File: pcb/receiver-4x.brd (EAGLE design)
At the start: 76.2 x 50.8 mm, 26 parts, among them IC1 MAX3095CEE

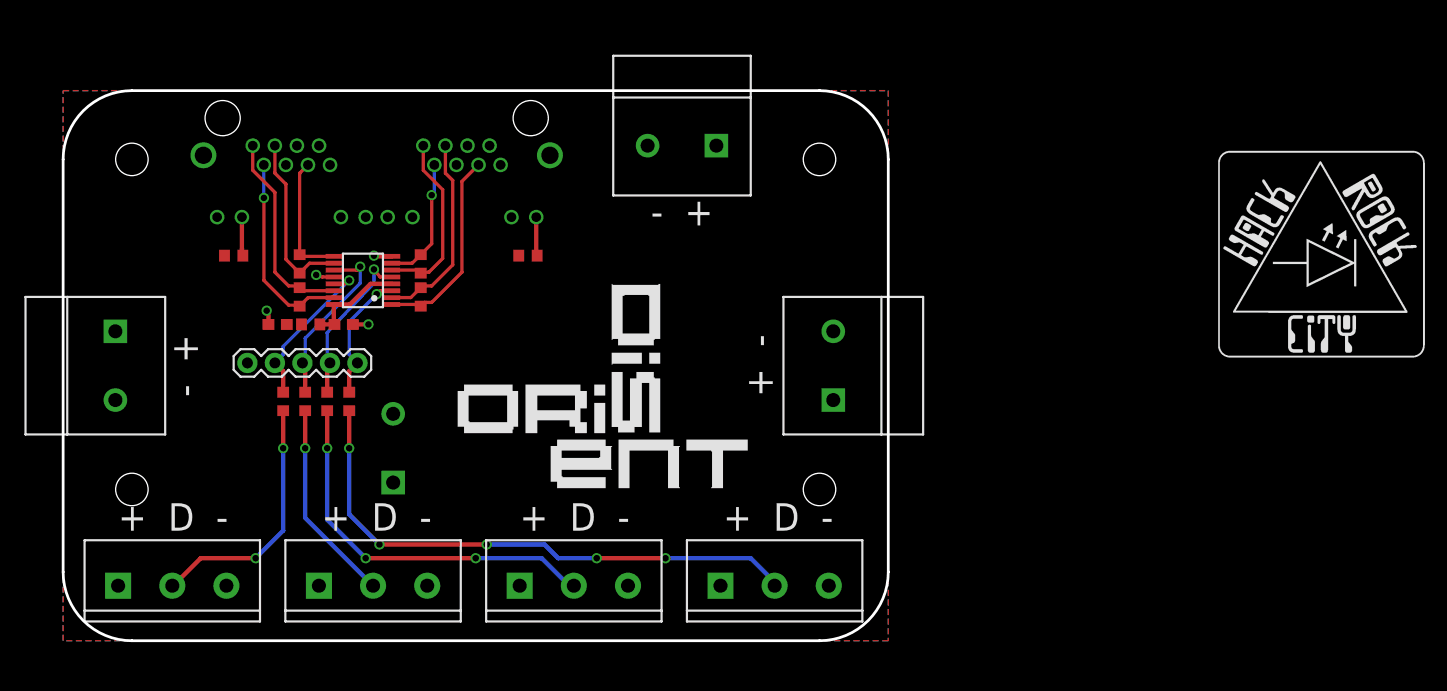
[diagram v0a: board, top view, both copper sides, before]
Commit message: Receiver 4x: Rev B design
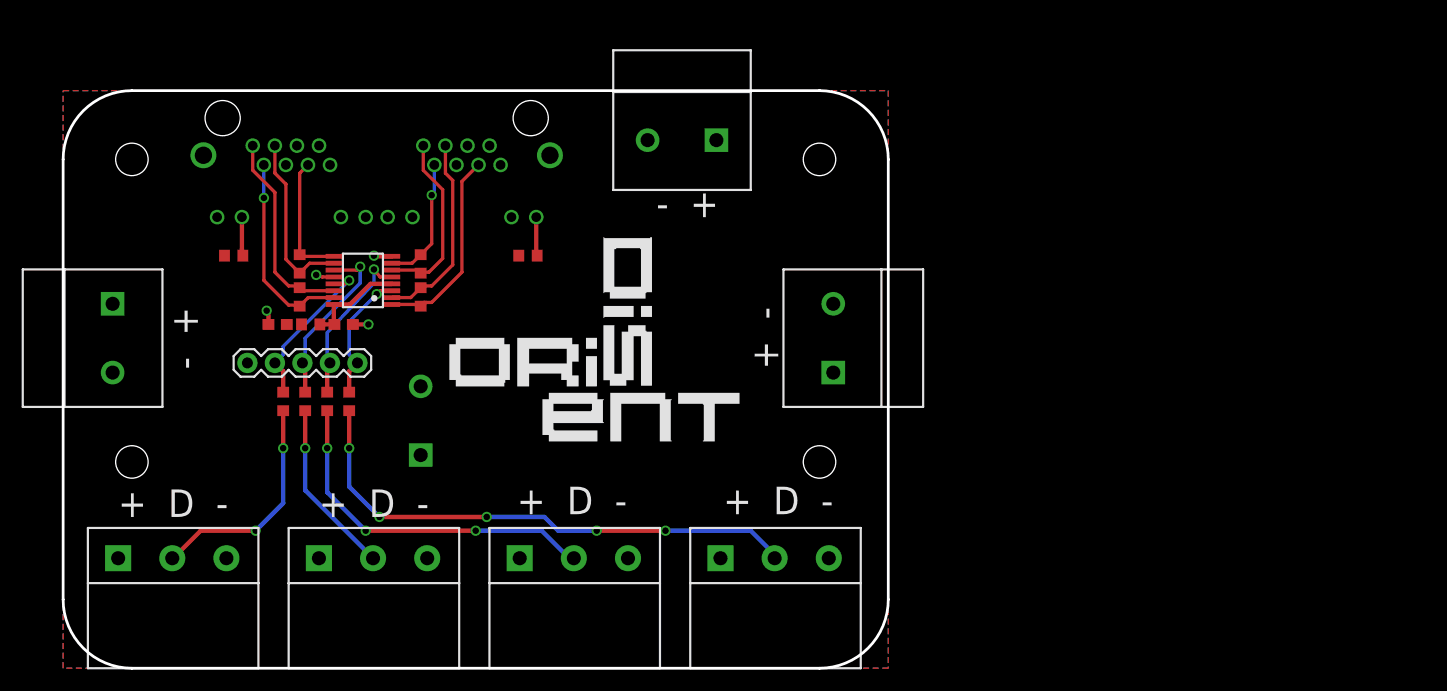
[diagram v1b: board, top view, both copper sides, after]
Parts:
- removed U$4: (no value), naim_misc:HRC_LOGO_0.75IN
- JP1, JP2, JP3, JP4: device SparkFun-Connectors:SCREWTERMINAL-5MM-3 -> LEDscape:SCREWTERMINAL-5MM-3-DETACHABLE
- moved U$3 4.38 mm to (49.5, 25.9)
- moved JP12 3.59 mm to (33.0, 20.3)
- moved JP5 2.55 mm to (4.57, 27.9)
- moved JP9 2.54 mm to (71.1, 27.9)
- moved JP1 2.54 mm to (60.7, 7.62)
- moved JP2 2.54 mm to (42.2, 7.62)
- moved JP3 2.54 mm to (23.6, 7.62)
- moved JP4 2.54 mm to (5.08, 7.62)
- moved JP10 0.51 mm to (57.1, 46.2)
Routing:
- net N$6: track 23.4 -> 20.9 mm
- net N$5: track 18.8 -> 16.2 mm
- net N$4: track 35.4 -> 32.8 mm
- net N$1: track 51.8 -> 49.2 mm
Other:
- board size 76.2 x 50.8 mm -> 76.2 x 53.3 mm
- board text added: "LEDscape receiver Rev B 2014-09-2 By Matt Mets"
- board text removed: "RS485 receiver Rev B 2014-09-1 @cibomahto"

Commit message: Updated BBB footprint, mounting holes in LEDscape baord, small cleanups
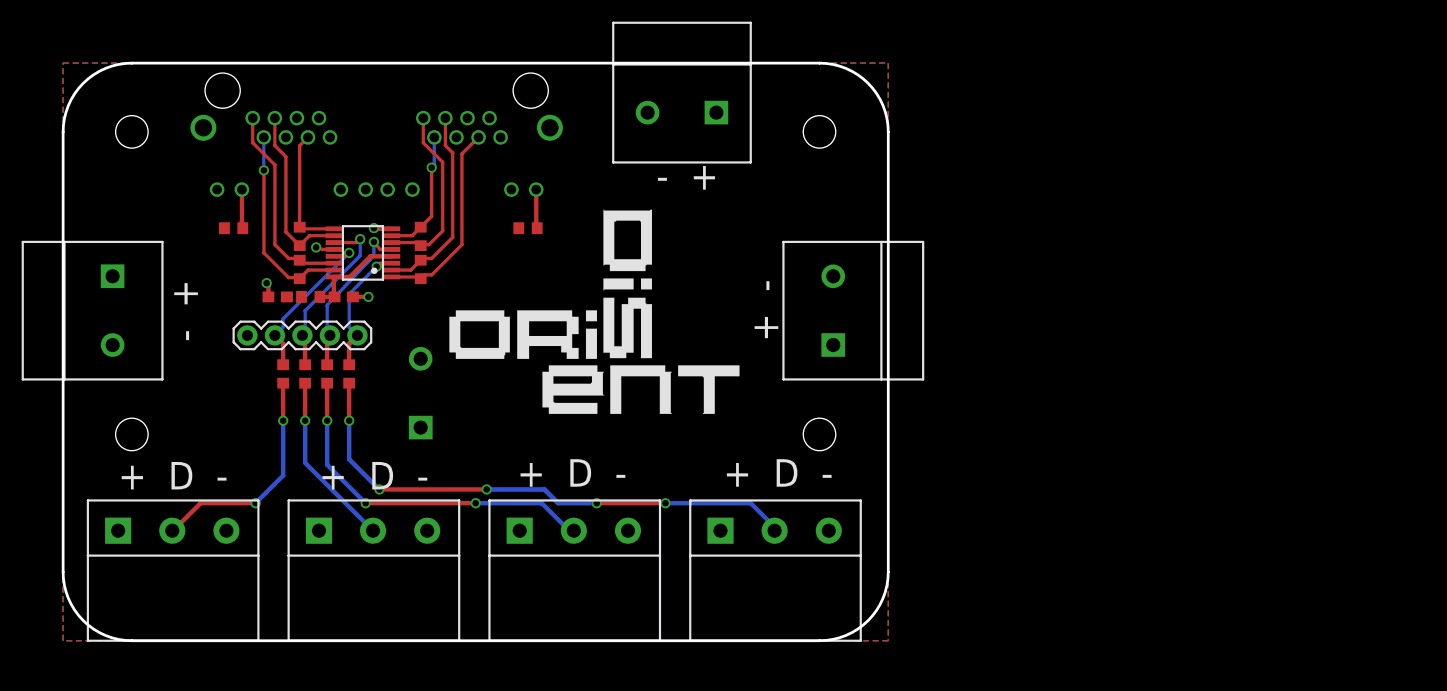
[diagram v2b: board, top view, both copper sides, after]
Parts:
- moved R1 2.54 mm to (26.4, 24.6)
- moved R2 2.54 mm to (24.4, 24.6)
- moved R3 2.54 mm to (22.4, 24.6)
- moved R4 2.54 mm to (20.3, 24.6)
- moved JP1 2.54 mm to (60.7, 10.2)
- moved JP2 2.54 mm to (42.2, 10.2)
- moved JP3 2.54 mm to (23.6, 10.2)
- moved JP4 2.54 mm to (5.08, 10.2)
- moved C1 2.54 mm to (25.9, 31.8)
- moved C2 2.54 mm to (19.8, 31.8)
- moved IC1 2.54 mm to (27.7, 35.8)
- moved JP10 2.54 mm to (57.1, 48.8)
- moved JP12 2.54 mm to (33.0, 22.9)
- moved JP5 2.54 mm to (4.57, 30.5)
- moved JP6 2.54 mm to (27.2, 28.2)
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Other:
- outline, holes or cut-outs redrawn
